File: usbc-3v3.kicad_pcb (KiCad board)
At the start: 2 copper layers, 48 x 30 mm, 15 parts, among them J1 HRO TYPE-C-31-M-12, J2 3V3_OUT, U1 AMS1117-3.3

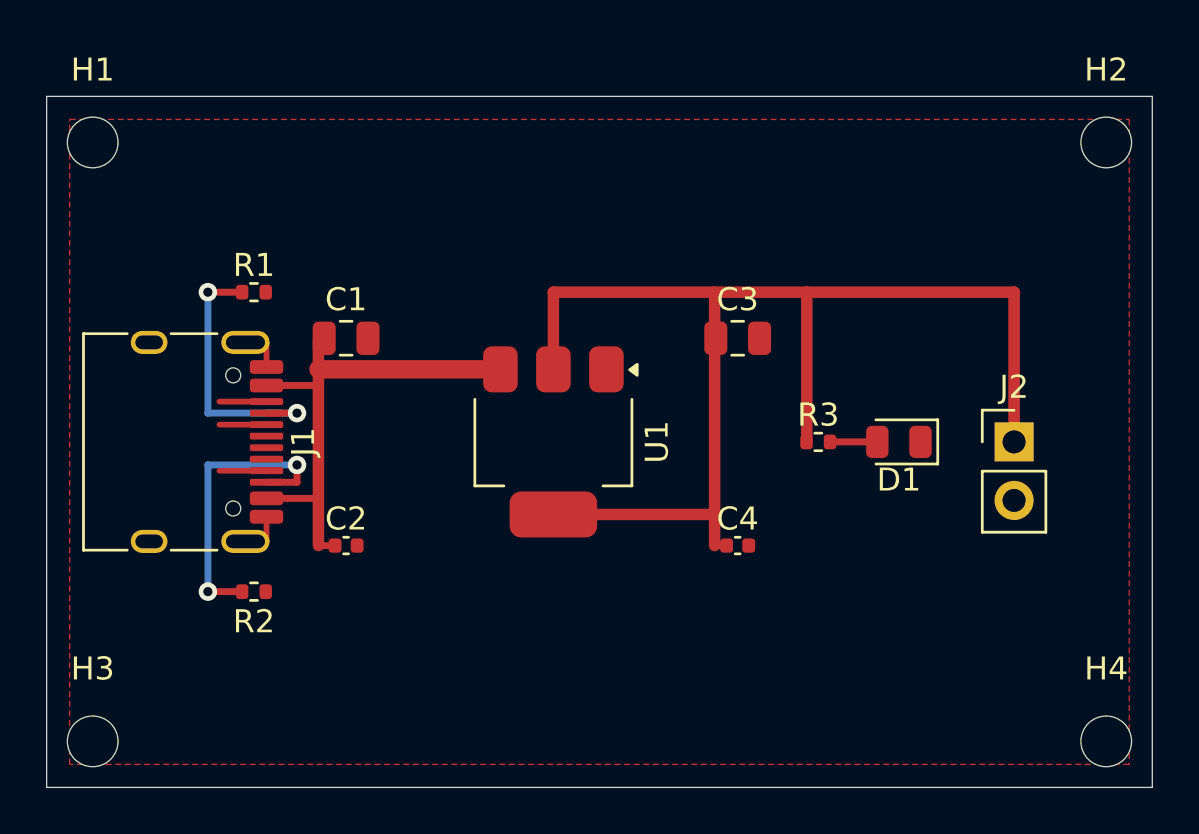
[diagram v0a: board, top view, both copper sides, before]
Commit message: feat: port to circuit_toolkit (three-file design pattern)
Replaces monolithic scripts/build_board.py with:
- circuit.py — topology in 25 lines using circuit_toolkit blocks
- layout.py — positions + tracks + vias + zones (extracted from existing PCB)
- build.py  — orchestrator (15 lines)

scripts/build_board.py kept as historical reference.

Outputs (verified via verify.sh --fab, 5/5 PASS):
- usbc-3v3.kicad_pcb (DRC: 0 errors, 44 cosmetic silk warnings)
- output/docs/schematic.svg (auto-generated by netlistsvg)
- output/fab/bom/{bom,bom_jlcpcb}.csv (with LCSC numbers)

verify.sh updated to distinguish DRC errors from warnings.

Round-trip workflow:
1. Edit circuit.py for topology / layout.py for positions
2. python build.py → produces .kicad_pcb
3. (Optional) tweak in KiCad GUI
4. python -m circuit_toolkit.builders.extract_layout usbc-3v3.kicad_pcb layout.py
5. layout.py 'positions' block updated; tracks/vias/zones preserved

Requires: kicad-claude-toolkit/python/circuit_toolkit installed in
KiCad's Python (https://github.com/nickleassdimebutt/kicad-claude-toolkit)

Co-Authored-By: Claude Sonnet 4.6 <noreply@anthropic.com>
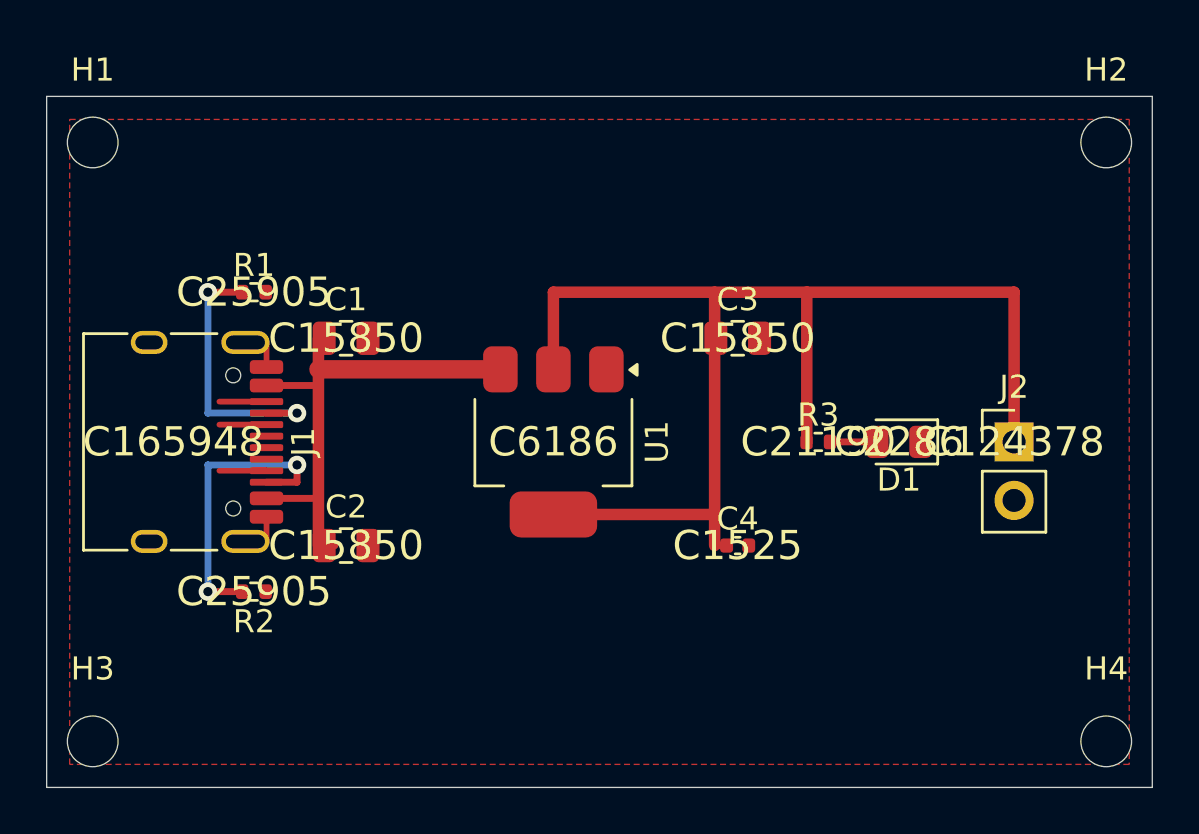
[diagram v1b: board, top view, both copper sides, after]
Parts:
- C1, C3: value 10uF/10V -> 10uF
- C2: value 100nF -> 10uF; footprint C_0402_1005Metric -> C_0805_2012Metric
- H1, H2, H3, H4: value M2 -> MountingHole_M2
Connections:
- net N_LED renamed N_D1
